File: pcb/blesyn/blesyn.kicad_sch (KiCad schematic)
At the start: 7 parts, among them J1 RJ12, U1 XIAO-ESP32-S3, U2 R-783.3-0.5

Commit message: PCB v1.0
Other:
- title: (none) -> blesyn
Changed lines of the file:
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@@
 	(generator_version "10.0")
 	(paper "A4")
+	(title_block
+		(title "blesyn")
+		(rev "1.0")
+	)
 	(junction
 		(at 158.75 99.06)

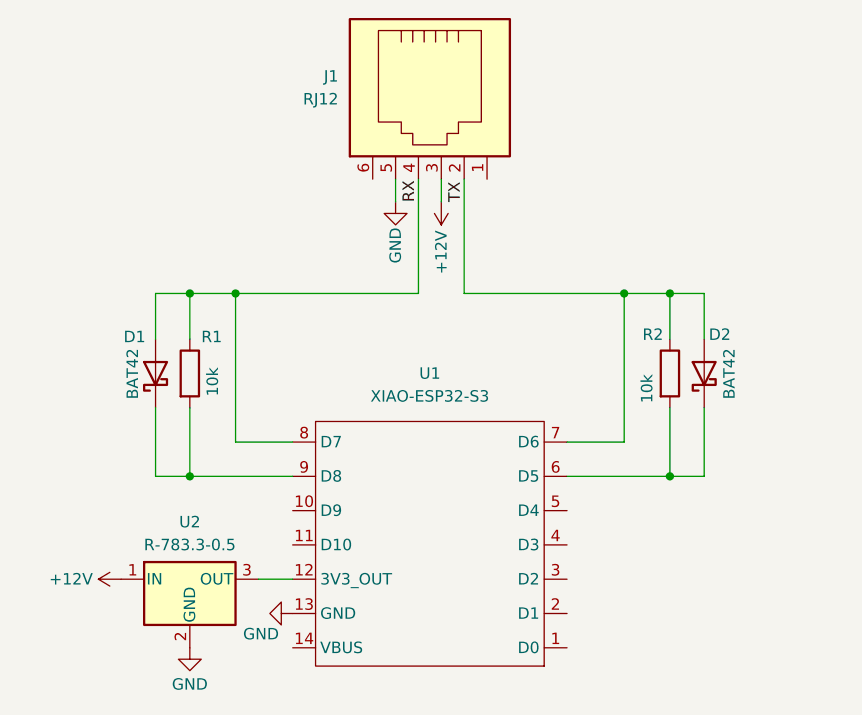
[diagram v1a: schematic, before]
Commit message: add SMD1206 handsoldering parts
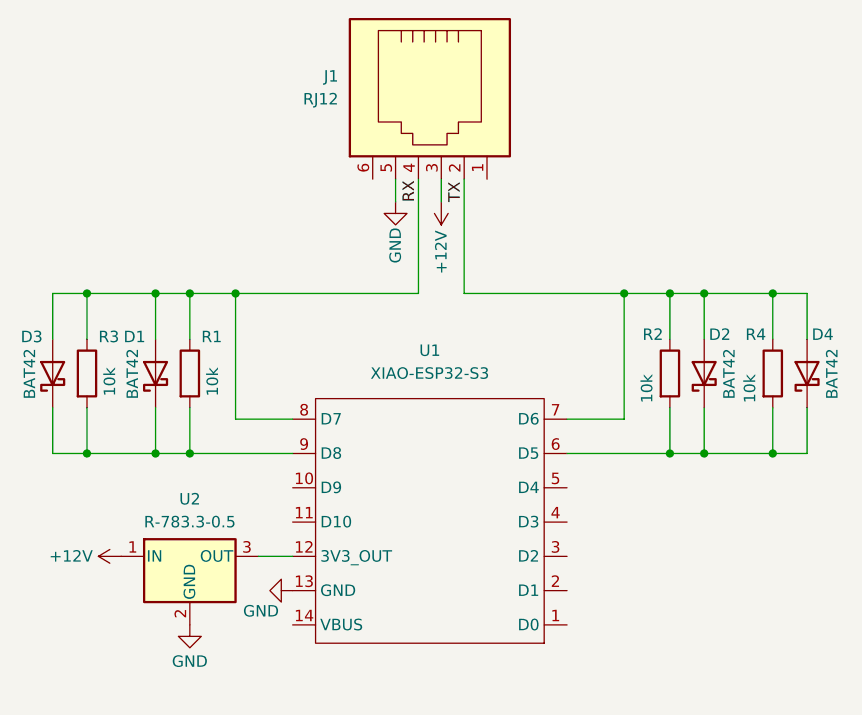
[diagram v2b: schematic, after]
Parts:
- added D3, D4: BAT42, Diode_SMD:D_1206_3216Metric_Pad1.42x1.75mm_HandSolder, symbol Device:D_Schottky
- added R3, R4: 10k, Resistor_SMD:R_1206_3216Metric_Pad1.30x1.75mm_HandSolder, symbol Device:R
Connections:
- net RX: now also D3.2 (A), R3.1
- net TX: now also D4.2 (A), R4.1
- net at D2.1 (K), R2.2, U1.6 (D5): now also D4.1 (K), R4.2
- net at D1.1 (K), R1.2, U1.9 (D8): now also D3.1 (K), R3.2
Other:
- moved on the sheet: U1, U2
